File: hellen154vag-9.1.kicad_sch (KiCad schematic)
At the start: 298 parts, among them J1 USB_B_Mini, J10 AudioJack_THR, J2 Conn_01x01, J3 Conn_01x01, J4 Conn_01x01, J5 Conn_01x01, J6 Conn_01x01, J7 Conn_01x04, J8 Conn_01x06, J9 Conn_01x04, M1 Module-can-0.1, M10 Module-can-0.1, M11 Module-vr-0.1, M12 Module-dinput4-0.1, M2 Module-power5-0.2, M3 Module-mcu-0.1, M4 Module-input-0.1, M5 Module-knock-0.1, M6 Module-output-0.1, M7 Module-ign8-0.1, M8 Module-power12-0.1, M9 Module-wbo-0.1, P1 368255-2, U1 L6205PD, U2 LPS25HB, U3 MCP6002-xSN

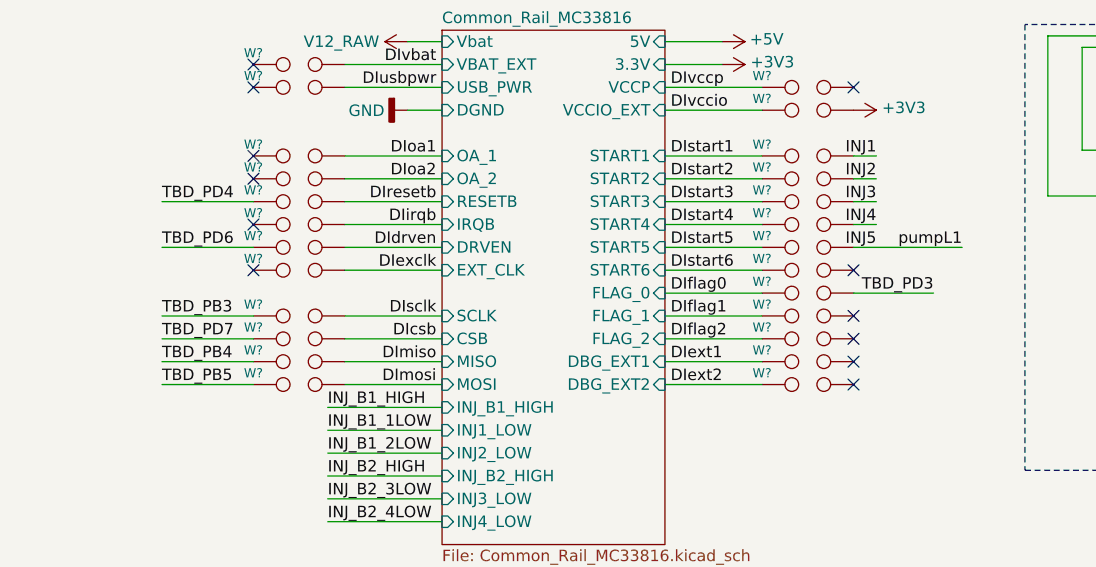
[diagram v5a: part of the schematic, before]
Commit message: Need to resolved TBD_###_or_### Two different potential pin outs found at the below, top of page and bottom of page have different pin-outs. https://github.com/rusefi/rusefi/wiki/MC33816-PT2001-dev-board
https://github.com/rusefi/hellen154vag-9.1/issues/4
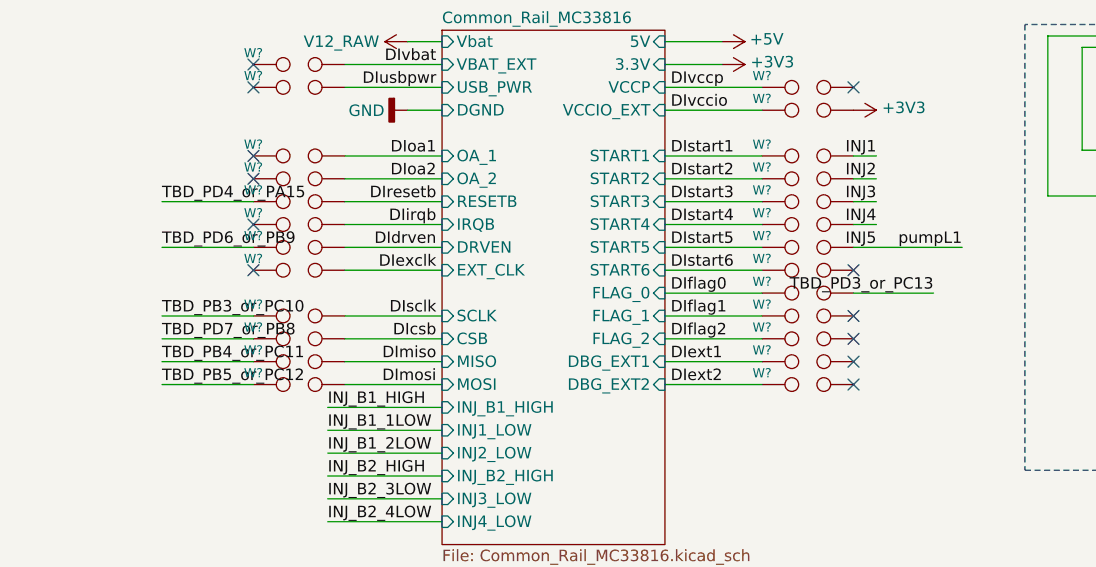
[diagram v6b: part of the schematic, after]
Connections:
- net TBD_PB3 renamed TBD_PB3_or_PC10
- net TBD_PB4 renamed TBD_PB4_or_PC11
- net TBD_PB5 renamed TBD_PB5_or_PC12
- net TBD_PD3 renamed TBD_PD3_or_PC13
- net TBD_PD4 renamed TBD_PD4_or_PA15
- net TBD_PD6 renamed TBD_PD6_or_PB9
- net TBD_PD7 renamed TBD_PD7_or_PB8
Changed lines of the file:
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@@
     (effects (font (size 1.27 1.27)) (justify left bottom))
   )
-  (label "TBD_PD4" (at 14.605 457.2 0)
-    (effects (font (size 1.27 1.27)) (justify left bottom))
-  )
-  (label "TBD_PD6" (at 14.605 462.28 0)
-    (effects (font (size 1.27 1.27)) (justify left bottom))
-  )
-  (label "TBD_PB3" (at 14.605 469.9 0)
-    (effects (font (size 1.27 1.27)) (justify left bottom))
-  )
-  (label "TBD_PD7" (at 14.605 472.44 0)
-    (effects (font (size 1.27 1.27)) (justify left bottom))
-  )
-  (label "TBD_PB4" (at 14.605 474.98 0)
-    (effects (font (size 1.27 1.27)) (justify left bottom))
-  )
-  (label "TBD_PB5" (at 14.605 477.52 0)
+  (label "TBD_PD4_or_PA15" (at 14.605 457.2 0)
+    (effects (font (size 1.27 1.27)) (justify left bottom))
+  )
+  (label "TBD_PD6_or_PB9" (at 14.605 462.28 0)
+    (effects (font (size 1.27 1.27)) (justify left bottom))
+  )
+  (label "TBD_PB3_or_PC10" (at 14.605 469.9 0)
+    (effects (font (size 1.27 1.27)) (justify left bottom))
+  )
+  (label "TBD_PD7_or_PB8" (at 14.605 472.44 0)
+    (effects (font (size 1.27 1.27)) (justify left bottom))
+  )
+  (label "TBD_PB4_or_PC11" (at 14.605 474.98 0)
+    (effects (font (size 1.27 1.27)) (justify left bottom))
+  )
+  (label "TBD_PB5_or_PC12" (at 14.605 477.52 0)
     (effects (font (size 1.27 1.27)) (justify left bottom))
   )
@@
     (effects (font (size 1.27 1.27)) (justify right bottom))
   )
-  (label "TBD_PD3" (at 100.33 467.36 180)
-    (effects (font (size 1.27 1.27)) (justify right bottom))
-  )
+  (label "TBD_PD3_or_PC13" (at 100.33 467.36 180)
+    (effects (font (size 1.27 1.27)) (justify right bottom))
+  )

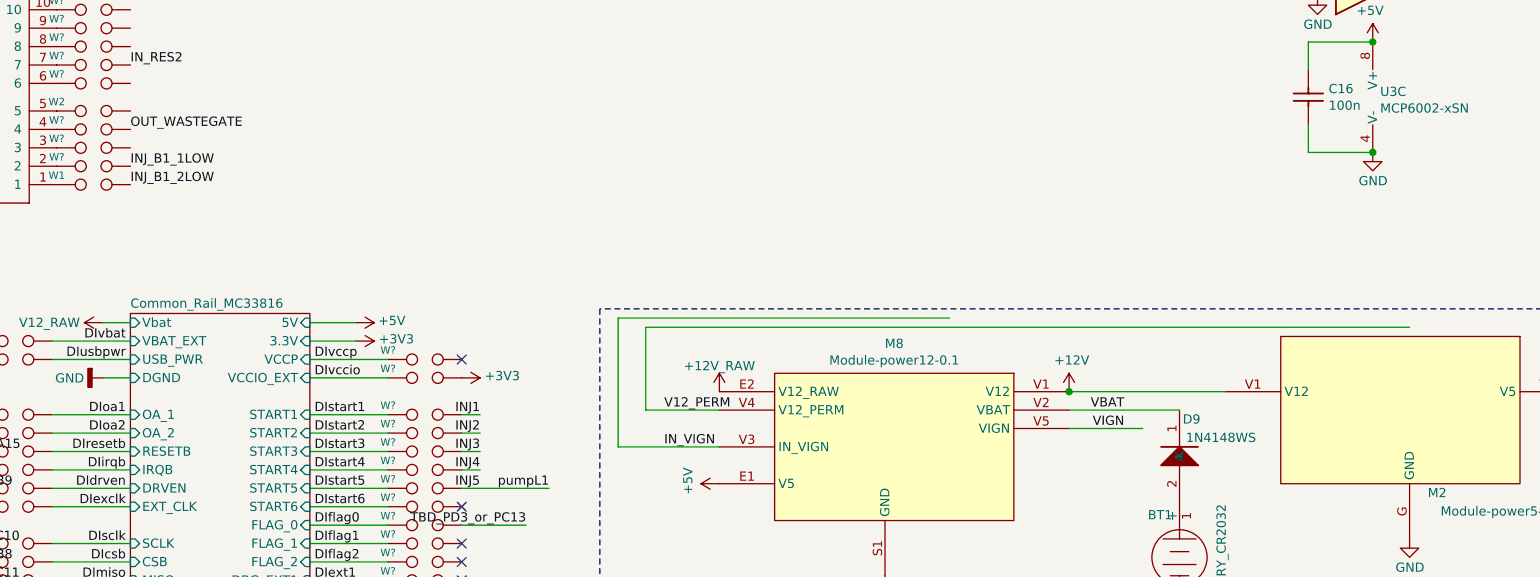
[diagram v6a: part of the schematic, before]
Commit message: JH does not see hot all times for 154, like 121 had. I made a best guess and added 0R W jumpers. 154 schematic found here https://github.com/rusefi/rusefi/wiki/VolkswagenPassatB6 121 schematic found here https://github.com/rusefi/rusefi/wiki/VAG-B5
https://github.com/rusefi/hellen154vag-9.1/issues/5
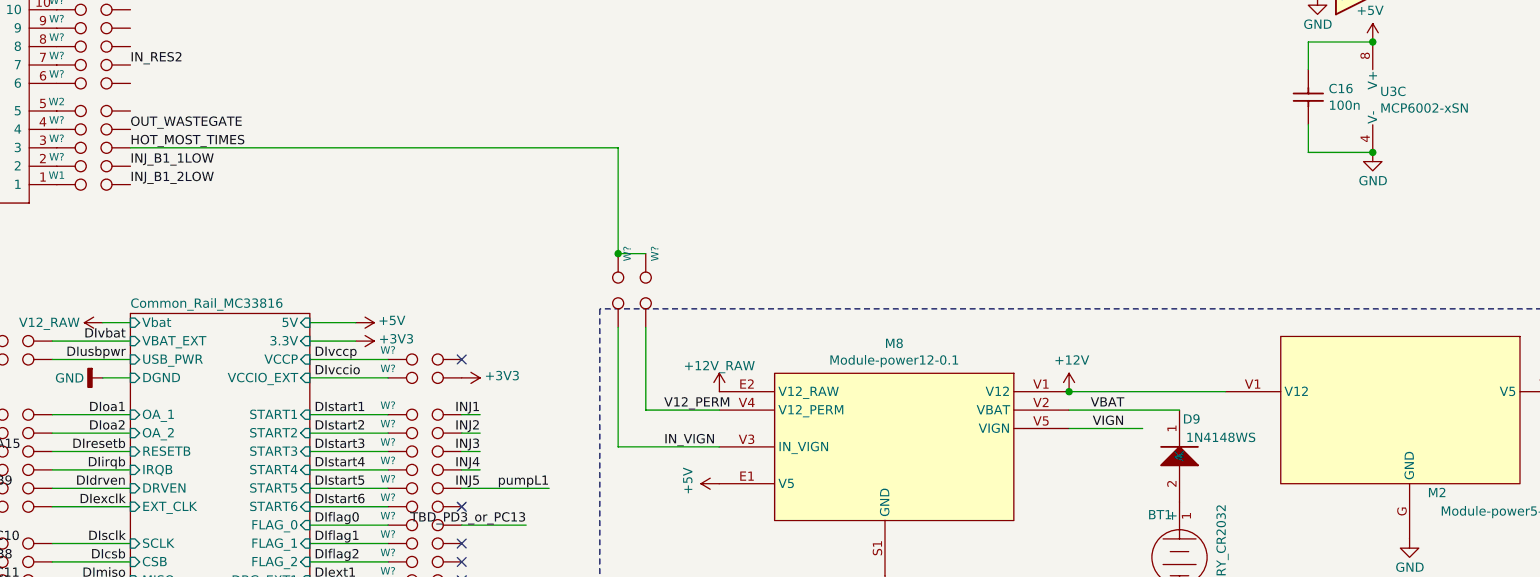
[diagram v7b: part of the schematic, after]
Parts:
- added W? (x2): TEST, rusEFI_Lib:SM0805_jumper, symbol hellen-one-common:TEST
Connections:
- net IN_VIGN: now also W?.2
- net V12_PERM: now also W?.2
- net HOT_MOST_TIMES: now reaches W?.2
- net HOT_MOST_TIMES: now also W?.1, W?.1
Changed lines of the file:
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@@
   (junction (at 55.245 522.605) (diameter 1.016) (color 0 0 0 0))
   (junction (at 55.245 537.845) (diameter 1.016) (color 0 0 0 0))
+  (junction (at 113.03 429.895) (diameter 1.016) (color 0 0 0 0))
   (junction (at 175.26 295.275) (diameter 1.016) (color 0 0 0 0))
   (junction (at 175.26 448.945) (diameter 1.016) (color 0 0 0 0))
@@
     (stroke (width 0) (type solid) (color 0 0 0 0))
   )
+  (wire (pts (xy 45.72 415.29) (xy 113.03 415.29))
+    (stroke (width 0) (type solid) (color 0 0 0 0))
+  )
   (wire (pts (xy 55.245 522.605) (xy 48.895 522.605))
     (stroke (width 0) (type solid) (color 0 0 0 0))
@@
     (stroke (width 0) (type solid) (color 0 0 0 0))
   )
-  (wire (pts (xy 113.03 438.785) (xy 158.75 438.785))
+  (wire (pts (xy 113.03 415.29) (xy 113.03 429.895))
     (stroke (width 0) (type solid) (color 0 0 0 0))
   )
-  (wire (pts (xy 113.03 456.565) (xy 113.03 438.785))
+  (wire (pts (xy 113.03 429.895) (xy 116.84 429.895))
     (stroke (width 0) (type solid) (color 0 0 0 0))
   )
-  (wire (pts (xy 113.03 456.565) (xy 127 456.565))
+  (wire (pts (xy 113.03 440.055) (xy 113.03 456.565))
     (stroke (width 0) (type solid) (color 0 0 0 0))
   )
-  (wire (pts (xy 116.84 440.055) (xy 116.84 451.485))
+  (wire (pts (xy 113.03 456.565) (xy 127 456.565))
     (stroke (width 0) (type solid) (color 0 0 0 0))
   )
-  (wire (pts (xy 116.84 440.055) (xy 222.25 440.055))
+  (wire (pts (xy 116.84 440.055) (xy 116.84 451.485))
     (stroke (width 0) (type solid) (color 0 0 0 0))
   )
@@
     (effects (font (size 1.27 1.27)) (justify left bottom))
   )
+  (label "HOT_MOST_TIMES" (at 45.72 415.29 0)
+    (effects (font (size 1.27 1.27)) (justify left bottom))
+  )
   (label "INJ_B1_1LOW" (at 45.72 417.83 0)
     (effects (font (size 1.27 1.27)) (justify left bottom))
@@
     (pin "2")
   )
+  (symbol (lib_id "hellen-one-common:TEST") (at 113.03 434.975 270) (unit 1)
+    (in_bom yes) (on_board yes)
+    (property "Reference" "W?" (id 0) (at 114.3 429.895 0)
+      (effects (font (size 1.016 1.016)))
+    )
+    (property "Value" "TEST" (id 1) (at 116.84 434.975 0)
+      (effects (font (size 1.016 1.016)) hide)
+    )
+    (property "Footprint" "rusEFI_Lib:SM0805_jumper" (id 2) (at 113.03 434.975 0)
+      (effects (font (size 1.524 1.524)) hide)
+    )
+    (property "Datasheet" "" (id 3) (at 113.03 434.975 0)
+      (effects (font (size 1.524 1.524)))
+    )
+    (pin "1")
+    (pin "2")
+  )
+  (symbol (lib_id "hellen-one-common:TEST") (at 116.84 434.975 270) (unit 1)
+    (in_bom yes) (on_board yes)
+    (property "Reference" "W?" (id 0) (at 118.11 429.895 0)
+      (effects (font (size 1.016 1.016)))
+    )
+    (property "Value" "TEST" (id 1) (at 120.65 434.975 0)
+      (effects (font (size 1.016 1.016)) hide)
+    )
+    (property "Footprint" "rusEFI_Lib:SM0805_jumper" (id 2) (at 116.84 434.975 0)
+      (effects (font (size 1.524 1.524)) hide)
+    )
+    (property "Datasheet" "" (id 3) (at 116.84 434.975 0)
+      (effects (font (size 1.524 1.524)))
+    )
+    (pin "1")
+    (pin "2")
+  )
   (symbol (lib_name "hellen-one-common:Pad_5") (lib_id "hellen-one-common:Pad") (at -412.115 163.195 0) (mirror x) (unit 1)
     (in_bom yes) (on_board yes)
@@
       (reference "W?") (unit 1) (value "TEST") (footprint "rusEFI_Lib:SM0805_jumper")
     )
+    (path "/266d26ab-a2e6-4d03-b438-45b101b3576a"
+      (reference "W?") (unit 1) (value "TEST") (footprint "rusEFI_Lib:SM0805_jumper")
+    )
     (path "/281607b2-ee03-4eac-953e-b21b94f7f7ae"
       (reference "W?") (unit 1) (value "TEST") (footprint "rusEFI_Lib:SM0805_jumper")
@@
       (reference "W?") (unit 1) (value "TEST") (footprint "rusEFI_Lib:SM0805_jumper")
     )
+    (path "/d3097088-9a42-4b76-b0b6-3f570b60afe4"
+      (reference "W?") (unit 1) (value "TEST") (footprint "rusEFI_Lib:SM0805_jumper")
+    )

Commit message: More nets connected, 2 are unresolved, TBD_PD4_or_PA15 and TBD_PD3_or_PC13. These IO are not connected to the STM32. Need to know what to connect them to. https://github.com/rusefi/hellen154vag-9.1/issues/4
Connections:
- net TBD_PB3_or_PC10 is gone; now on net SPI3_SCK: W?.1
- net TBD_PB4_or_PC11 is gone; now on net SPI3_MISO: W?.1
- net TBD_PB5_or_PC12 is gone; now on net SPI3_MOSI: W?.1
- net TBD_PD6_or_PB9 is gone; now on net DRVEN: W?.1
- net TBD_PD7_or_PB8 is gone; now on net SPI3_CS: W?.1
- net SPI3_MISO: now reaches M3.N10 (SPI3_MISO)
- net SPI3_MOSI: now reaches M3.N11 (SPI3_MOSI)
- net DRVEN: now reaches M3.N7 (UART2_RX)
- net SPI3_CS: now reaches M3.N8 (SPI3_CS)
- net SPI3_SCK: now reaches M3.N9 (SPI3_SCK)
- no-connect marks 84 -> 79
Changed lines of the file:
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@@
   (no_connect (at 330.2 90.805))
   (no_connect (at 330.2 93.345))
-  (no_connect (at 330.2 121.285))
-  (no_connect (at 330.2 123.825))
-  (no_connect (at 330.2 126.365))
-  (no_connect (at 330.2 128.905))
   (no_connect (at 330.2 159.385))
   (no_connect (at 330.2 161.925))
-  (no_connect (at 330.2 167.005))
   (no_connect (at 330.2 169.545))
   (no_connect (at 330.2 179.705))
@@
     (stroke (width 0) (type solid) (color 0 0 0 0))
   )
+  (wire (pts (xy 330.2 121.285) (xy 341.63 121.285))
+    (stroke (width 0) (type solid) (color 0 0 0 0))
+  )
+  (wire (pts (xy 330.2 123.825) (xy 341.63 123.825))
+    (stroke (width 0) (type solid) (color 0 0 0 0))
+  )
+  (wire (pts (xy 330.2 126.365) (xy 341.63 126.365))
+    (stroke (width 0) (type solid) (color 0 0 0 0))
+  )
+  (wire (pts (xy 330.2 128.905) (xy 341.63 128.905))
+    (stroke (width 0) (type solid) (color 0 0 0 0))
+  )
   (wire (pts (xy 330.2 139.065) (xy 341.63 139.065))
     (stroke (width 0) (type solid) (color 0 0 0 0))
@@
     (stroke (width 0) (type solid) (color 0 0 0 0))
   )
+  (wire (pts (xy 330.2 167.005) (xy 337.185 167.005))
+    (stroke (width 0) (type solid) (color 0 0 0 0))
+  )
   (wire (pts (xy 330.2 174.625) (xy 342.9 174.625))
     (stroke (width 0) (type solid) (color 0 0 0 0))
@@
     (effects (font (size 1.27 1.27)) (justify left bottom))
   )
-  (label "TBD_PD6_or_PB9" (at 14.605 462.28 0)
+  (label "DRVEN" (at 14.605 462.28 0)
     (effects (font (size 1.27 1.27)) (justify left bottom))
   )
-  (label "TBD_PB3_or_PC10" (at 14.605 469.9 0)
+  (label "SPI3_SCK" (at 14.605 469.9 0)
     (effects (font (size 1.27 1.27)) (justify left bottom))
   )
-  (label "TBD_PD7_or_PB8" (at 14.605 472.44 0)
+  (label "SPI3_CS" (at 14.605 472.44 0)
     (effects (font (size 1.27 1.27)) (justify left bottom))
   )
-  (label "TBD_PB4_or_PC11" (at 14.605 474.98 0)
+  (label "SPI3_MISO" (at 14.605 474.98 0)
     (effects (font (size 1.27 1.27)) (justify left bottom))
   )
-  (label "TBD_PB5_or_PC12" (at 14.605 477.52 0)
+  (label "SPI3_MOSI" (at 14.605 477.52 0)
     (effects (font (size 1.27 1.27)) (justify left bottom))
   )
@@
     (effects (font (size 1.27 1.27)) (justify right bottom))
   )
+  (label "DRVEN" (at 337.185 167.005 180)
+    (effects (font (size 1.27 1.27)) (justify right bottom))
+  )
   (label "SPI2_SCK" (at 341.63 103.505 180)
     (effects (font (size 1.27 1.27)) (justify right bottom))
@@
     (effects (font (size 1.27 1.27)) (justify right bottom))
   )
+  (label "SPI3_SCK" (at 341.63 121.285 180)
+    (effects (font (size 1.27 1.27)) (justify right bottom))
+  )
+  (label "SPI3_MISO" (at 341.63 123.825 180)
+    (effects (font (size 1.27 1.27)) (justify right bottom))
+  )
+  (label "SPI3_MOSI" (at 341.63 126.365 180)
+    (effects (font (size 1.27 1.27)) (justify right bottom))
+  )
+  (label "SPI3_CS" (at 341.63 128.905 180)
+    (effects (font (size 1.27 1.27)) (justify right bottom))
+  )
